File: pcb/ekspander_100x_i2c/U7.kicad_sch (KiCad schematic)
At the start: 39 parts, among them J18 DG127A-5.08-06P-14-00AH, J19 DG127A-5.08-06P-14-00AH, J20 DG127A-5.08-06P-14-00AH, J21 DG127A-5.08-06P-14-00AH, J22 DG127A-5.08-06P-14-00AH, J23 DG127A-5.08-06P-14-00AH, U34 LTV-847, U35 ITS716G, U36 ITS716G, U37 LTV-847, U38 ITS716G, U40 LTV-847, U7 MCP23017_SP, U8 MCP23017_SP

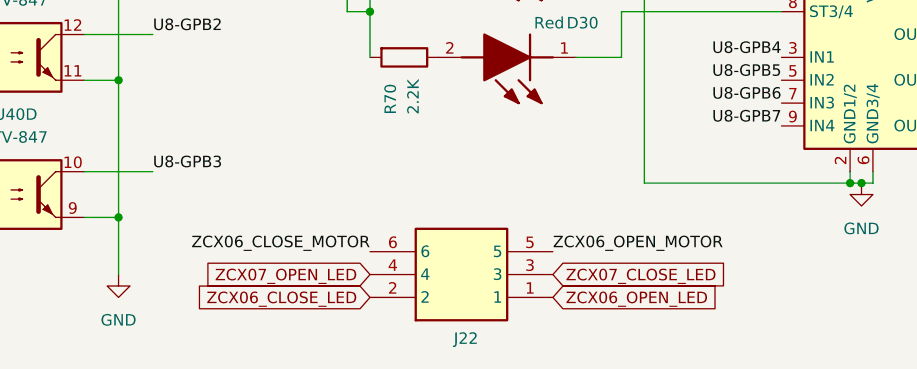
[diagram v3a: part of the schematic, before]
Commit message: Ekspander 100x - RS485
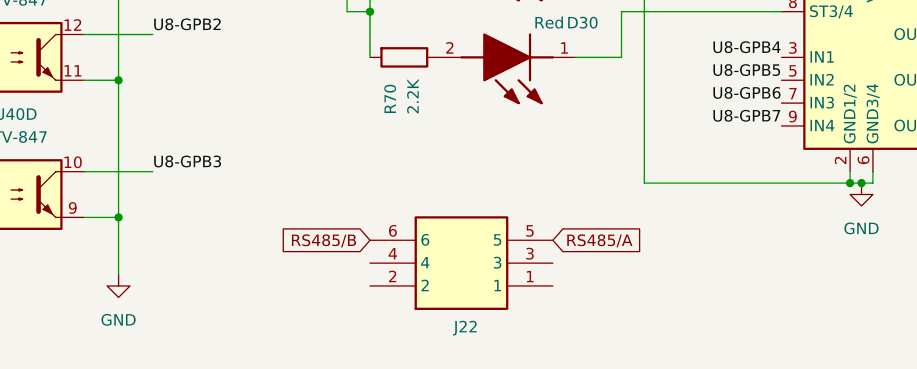
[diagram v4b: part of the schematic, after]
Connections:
- net ZCX06_CLOSE_LED: no longer names the net of J22.2
- net ZCX06_CLOSE_MOTOR renamed RS485/B
- net ZCX06_OPEN_LED: no longer names the net of J22.1
- net ZCX06_OPEN_MOTOR renamed RS485/A
- net ZCX07_CLOSE_LED: no longer names the net of J22.3
- net ZCX07_OPEN_LED: no longer names the net of J22.4
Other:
- moved on the sheet: J22
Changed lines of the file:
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@@
 		)
 	)
-	(label "ZCX06_OPEN_MOTOR"
-		(at 105.41 187.96 0)
-		(fields_autoplaced yes)
-		(effects
-			(font
-				(size 1.27 1.27)
-			)
-			(justify left bottom)
-		)
-		(property "Netclass" "+24V"
-			(at 105.41 189.23 0)
-			(effects
-				(font
-					(size 1.27 1.27)
-					(italic yes)
-				)
-				(justify left)
-				(hide yes)
-			)
-		)
-	)
 	(label "U7-GPB0"
 		(at 69.85 31.75 0)
@@
 		)
 	)
-	(label "ZCX06_CLOSE_MOTOR"
-		(at 85.09 187.96 180)
-		(fields_autoplaced yes)
-		(effects
-			(font
-				(size 1.27 1.27)
-			)
-			(justify right bottom)
-		)
-		(property "Netclass" "+24V"
-			(at 85.09 189.23 0)
-			(effects
-				(font
-					(size 1.27 1.27)
-					(italic yes)
-				)
-				(justify right)
-				(hide yes)
-			)
-		)
-	)
 	(label "U7-GPA1"
 		(at 269.24 133.35 0)
@@
 		)
 	)
-	(global_label "ZCX07_OPEN_LED"
-		(shape input)
-		(at 85.09 190.5 180)
-		(fields_autoplaced yes)
-		(effects
-			(font
-				(size 1.27 1.27)
-			)
-			(justify right)
-		)
-		(property "Intersheetrefs" "${INTERSHEET_REFS}"
-			(at 64.6274 190.5 0)
-			(effects
-				(font
-					(size 1.27 1.27)
-				)
-				(justify right)
-				(hide yes)
-			)
-		)
-	)
 	(global_label "ZCX01_OPEN_LED"
 		(shape input)
@@
 		)
 	)
+	(global_label "RS485{slash}A"
+		(shape input)
+		(at 105.41 186.69 0)
+		(fields_autoplaced yes)
+		(effects
+			(font
+				(size 1.27 1.27)
+			)
+			(justify left)
+		)
+		(property "Intersheetrefs" "${INTERSHEET_REFS}"
+			(at 117.1037 186.69 0)
+			(effects
+				(font
+					(size 1.27 1.27)
+				)
+				(justify left)
+				(hide yes)
+			)
+		)
+	)
 	(global_label "ZCX01_CLOSE_LED"
 		(shape input)
@@
 		)
 	)
-	(global_label "ZCX07_CLOSE_LED"
-		(shape input)
-		(at 105.41 190.5 0)
-		(fields_autoplaced yes)
-		(effects
-			(font
-				(size 1.27 1.27)
-			)
-			(justify left)
-		)
-		(property "Intersheetrefs" "${INTERSHEET_REFS}"
-			(at 124.9655 190.5 0)
-			(effects
-				(font
-					(size 1.27 1.27)
-				)
-				(justify left)
-				(hide yes)
-			)
-		)
-	)
 	(global_label "U7-GPB6"
 		(shape input)
@@
 		)
 	)
-	(global_label "ZCX06_OPEN_LED"
-		(shape input)
-		(at 105.41 193.04 0)
-		(fields_autoplaced yes)
-		(effects
-			(font
-				(size 1.27 1.27)
-			)
-			(justify left)
-		)
-		(property "Intersheetrefs" "${INTERSHEET_REFS}"
-			(at 124.9655 193.04 0)
-			(effects
-				(font
-					(size 1.27 1.27)
-				)
-				(justify left)
-				(hide yes)
-			)
-		)
-	)
 	(global_label "U7-GPB4"
 		(shape input)
@@
 		)
 	)
+	(global_label "RS485{slash}B"
+		(shape input)
+		(at 85.09 186.69 180)
+		(fields_autoplaced yes)
+		(effects
+			(font
+				(size 1.27 1.27)
+			)
+			(justify right)
+		)
+		(property "Intersheetrefs" "${INTERSHEET_REFS}"
+			(at 73.5777 186.69 0)
+			(effects
+				(font
+					(size 1.27 1.27)
+				)
+				(justify right)
+				(hide yes)
+			)
+		)
+	)
 	(global_label "ZCX02_CLOSE_LED"
 		(shape input)
@@
 		)
 	)
-	(global_label "ZCX06_CLOSE_LED"
-		(shape input)
-		(at 85.09 193.04 180)
-		(fields_autoplaced yes)
-		(effects
-			(font
-				(size 1.27 1.27)
-			)
-			(justify right)
-		)
-		(property "Intersheetrefs" "${INTERSHEET_REFS}"
-			(at 64.6274 193.04 0)
-			(effects
-				(font
-					(size 1.27 1.27)
-				)
-				(justify right)
-				(hide yes)
-			)
-		)
-	)
 	(global_label "SCK"
 		(shape input)
@@
 	(symbol
 		(lib_id "1_tme:DG127A-5.08-06P-14-00AH")
-		(at 85.09 193.04 0)
+		(at 85.09 191.77 0)
 		(mirror x)
 		(unit 1)
@@
 		(dnp no)
 		(property "Reference" "J22"
-			(at 95.758 197.612 0)
+			(at 95.758 196.342 0)
 			(effects
 				(font
@@
 		)
 		(property "Value" "DG127A-5.08-06P-14-00AH"
-			(at 95.758 181.356 0)
+			(at 95.758 180.086 0)
 			(effects
 				(font
@@
 		)
 		(property "Footprint" "DG127A50806P1400AH"
-			(at 101.6 98.12 0)
+			(at 101.6 96.85 0)
 			(effects
 				(font
@@
 		)
 		(property "Datasheet" "https://www.degson.com/index.php?a=downloadFile&id=1094971&name=%27ZmlsZTQ=%27&lang=en"
-			(at 101.6 -1.88 0)
+			(at 101.6 -3.15 0)
 			(effects
 				(font
@@
 		)
 		(property "Description" "PCB terminal block; angled 90; 5.08mm; ways: 6; on PCBs; terminal"
-			(at 85.09 193.04 0)
+			(at 85.09 191.77 0)
 			(effects
 				(font
@@
 		)
 		(property "Height" "19.41"
-			(at 101.6 -201.88 0)
+			(at 101.6 -203.15 0)
 			(effects
 				(font
@@
 		)
 		(property "TME Electronic Components Part Number" ""
-			(at 101.6 -301.88 0)
+			(at 101.6 -303.15 0)
 			(effects
 				(font
@@
 		)
 		(property "TME Electronic Components Price/Stock" ""
-			(at 101.6 -401.88 0)
+			(at 101.6 -403.15 0)
 			(effects
 				(font
@@
 		)
 		(property "Manufacturer_Name" "Degson"
-			(at 101.6 -501.88 0)
+			(at 101.6 -503.15 0)
 			(effects
 				(font
@@
 		)
 		(property "Manufacturer_Part_Number" "DG127A-5.08-06P-14-00AH"
-			(at 101.6 -601.88 0)
+			(at 101.6 -603.15 0)
 			(effects
 				(font
